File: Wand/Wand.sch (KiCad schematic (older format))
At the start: 20 parts, among them P1 ISP, P2 KLB4, P3 BASE, U1 ATMEGA328-MMH, U2 MAX31855KASA+, U3 MPU-6050

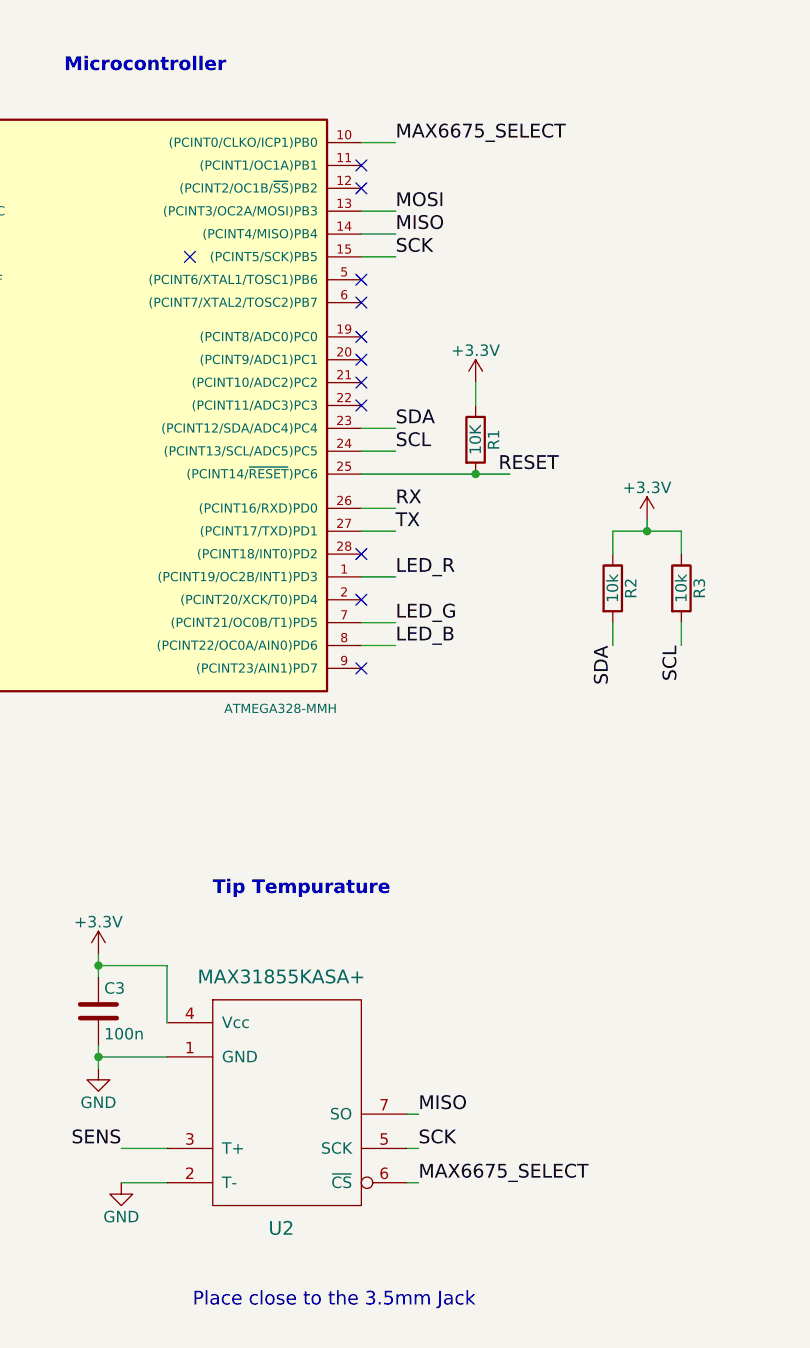
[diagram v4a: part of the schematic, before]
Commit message: Corrected the MAX31855 chip select line, should be D10 (pin 12) not pin 10
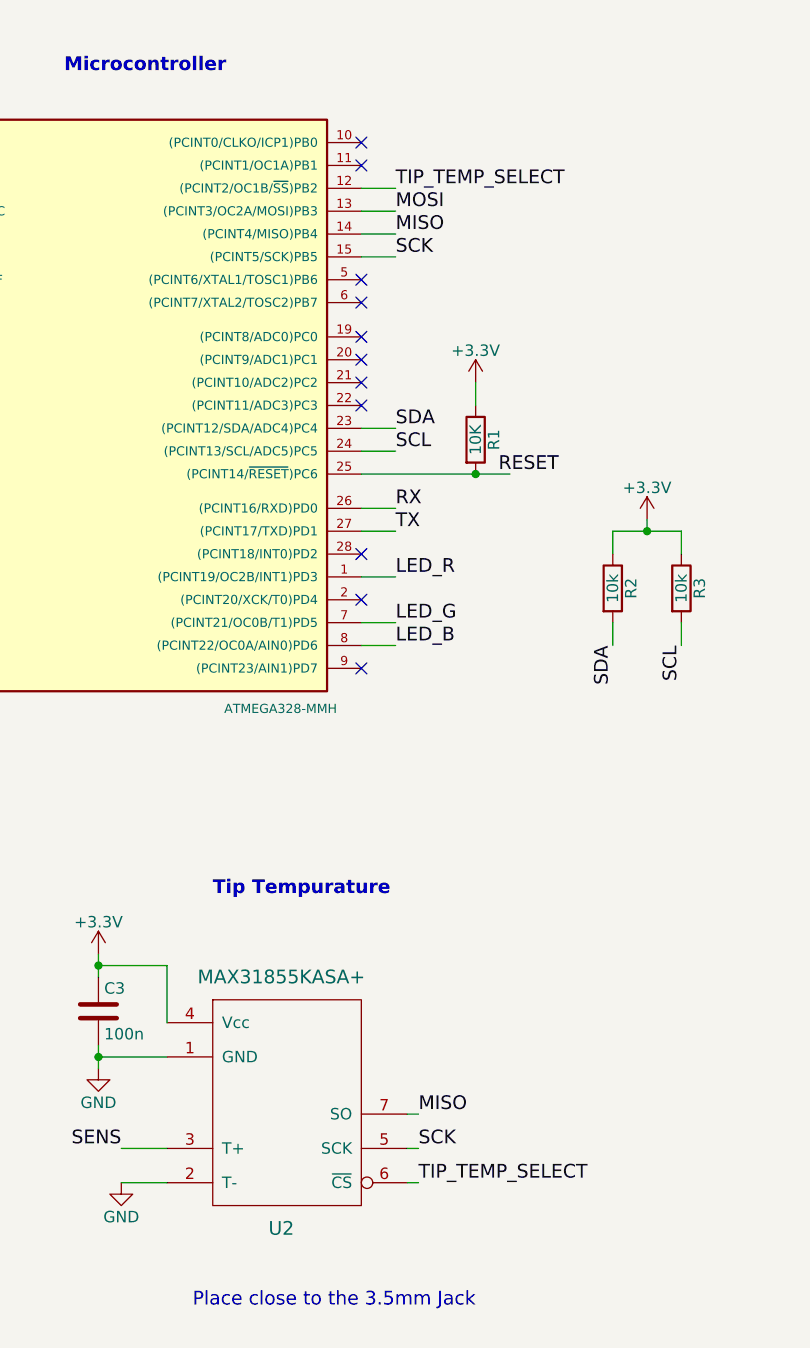
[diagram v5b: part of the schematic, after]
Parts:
- P2: footprint Wand:Reichelt_EBS35 -> SMD_Packages:Conn-3
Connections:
- net TIP_TEMP_SELECT: now reaches U1.12 ((PCINT2/OC1B/~SS~)PB2)
- net TIP_TEMP_SELECT: now also U2.6 (~CS)
- net MAX6675_SELECT: no longer names the net of U1.10 ((PCINT0/CLKO/ICP1)PB0)
- net MAX6675_SELECT: no longer U2.6 (~CS)
- no-connect marks 15 -> 14
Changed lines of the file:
@@
 F 0 "P2" H 10000 5250 50  0000 C CNN
 F 1 "KLB4" H 9950 4700 50  0000 C CNN
-F 2 "Wand:Reichelt_EBS35" H 10100 4850 60  0001 C CNN
+F 2 "SMD_Packages:Conn-3" H 10100 4850 60  0001 C CNN
 F 3 "" H 10100 4850 60  0000 C CNN
 	1    10000 5000
@@
 NoConn ~ 3450 2500
 NoConn ~ 3450 2400
-NoConn ~ 3450 1650
 NoConn ~ 3450 1550
 NoConn ~ 8400 2000
@@
 NoConn ~ 3450 2050
 NoConn ~ 3450 2150
-NoConn ~ 2700 1950
 $Comp
 L R R1
@@
 SCK
 Text Label 3700 6000 0    60   ~ 0
-MAX6675_SELECT
+TIP_TEMP_SELECT
 Wire Wire Line
 	3650 6000 3700 6000
@@
 Wire Wire Line
 	3650 5700 3700 5700
-Text Label 3600 1450 0    60   ~ 0
-MAX6675_SELECT
-Wire Wire Line
-	3600 1450 3450 1450
+Text Label 3600 1650 0    60   ~ 0
+TIP_TEMP_SELECT
+Wire Wire Line
+	3600 1650 3450 1650
 Wire Wire Line
 	1550 3750 1400 3750
@@
 Text Notes 7050 6700 0    60   ~ 12
 Hotstick Wand
+NoConn ~ 3450 1450
 $EndSCHEMATC

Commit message: Custom footprints for the base and 3.5mm Jack
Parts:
- P2: footprint SMD_Packages:Conn-3 -> Wand:Jack_3.5mm_KLB
- P3: footprint Pin_Headers:Pin_Header_Straight_1x05 -> Wand:Base_Connector
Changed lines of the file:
@@
 F 0 "P2" H 10000 5250 50  0000 C CNN
 F 1 "KLB4" H 9950 4700 50  0000 C CNN
-F 2 "SMD_Packages:Conn-3" H 10100 4850 60  0001 C CNN
+F 2 "Wand:Jack_3.5mm_KLB" H 10100 4850 60  0001 C CNN
 F 3 "" H 10100 4850 60  0000 C CNN
 	1    10000 5000
@@
 F 0 "P3" H 10200 2200 50  0000 C CNN
 F 1 "BASE" V 10300 1900 50  0000 C CNN
-F 2 "Pin_Headers:Pin_Header_Straight_1x05" H 10200 1900 60  0001 C CNN
+F 2 "Wand:Base_Connector" H 10200 1900 60  0001 C CNN
 F 3 "" H 10200 1900 60  0000 C CNN
 	1    10200 1900

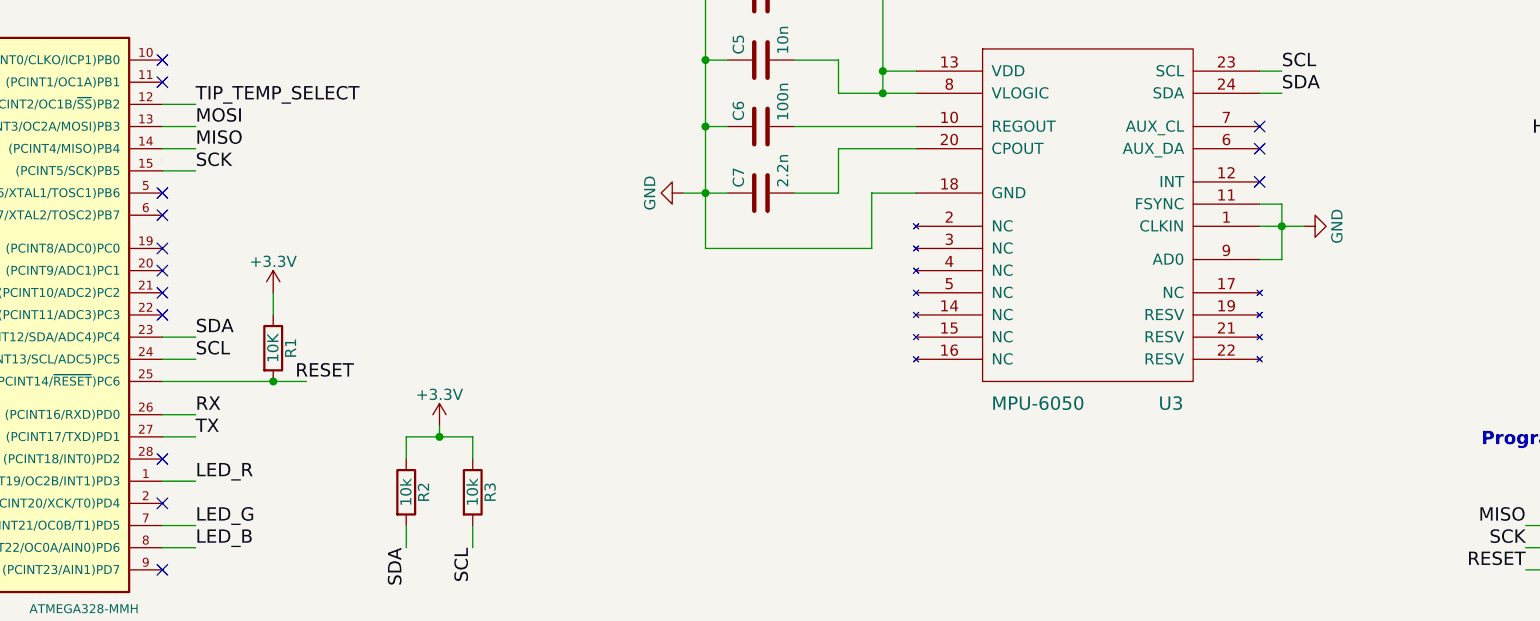
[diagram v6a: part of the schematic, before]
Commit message: Connected the MPU interrupt, needed by the http://www.i2cdevlib.com/ library for the MPU-6050
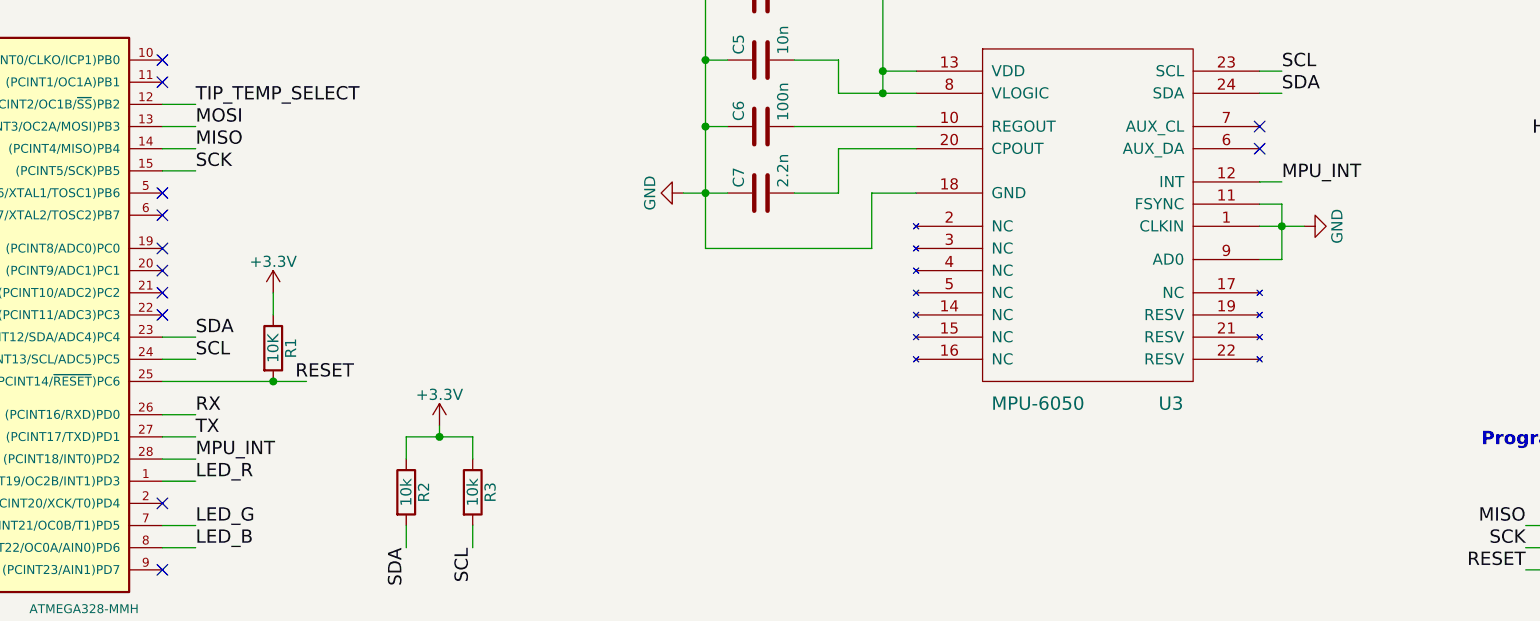
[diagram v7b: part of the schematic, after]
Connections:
- net MPU_INT: now reaches U1.28 ((PCINT18/INT0)PD2)
- net MPU_INT: now also U3.12 (INT)
- no-connect marks 14 -> 12
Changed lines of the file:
@@
 NoConn ~ 3450 3750
 NoConn ~ 3450 3450
-NoConn ~ 3450 3250
 NoConn ~ 3450 2600
 NoConn ~ 3450 2500
 NoConn ~ 3450 2400
 NoConn ~ 3450 1550
-NoConn ~ 8400 2000
 NoConn ~ 8400 1850
 NoConn ~ 8400 1750
@@
 Hotstick Wand
 NoConn ~ 3450 1450
+Text Label 8500 2000 0    60   ~ 0
+MPU_INT
+Wire Wire Line
+	8400 2000 8500 2000
+Text Label 3600 3250 0    60   ~ 0
+MPU_INT
+Wire Wire Line
+	3450 3250 3600 3250
 $EndSCHEMATC

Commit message: Initial PCB layout, still work in progress.
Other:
- note removed: "Hotstick Wand"
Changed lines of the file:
@@
 encoding utf-8
 Sheet 1 1
-Title ""
-Date ""
-Rev ""
-Comp ""
+Title "Hotstick Wand"
+Date "2016-01-20"
+Rev "1"
+Comp "rLab/Reading Hackspace"
 Comment1 ""
 Comment2 ""
@@
 Text Notes 8250 5800 0    60   ~ 0
 HEAT and GND traces between the Base unit connector and \nTip connector need to be able to carry 5A so trace needs to \nbe a minimum of 4mm
-Text Notes 7050 6700 0    60   ~ 12
-Hotstick Wand
 NoConn ~ 3450 1450
 Text Label 8500 2000 0    60   ~ 0
